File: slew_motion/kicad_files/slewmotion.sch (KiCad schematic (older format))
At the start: 115 parts

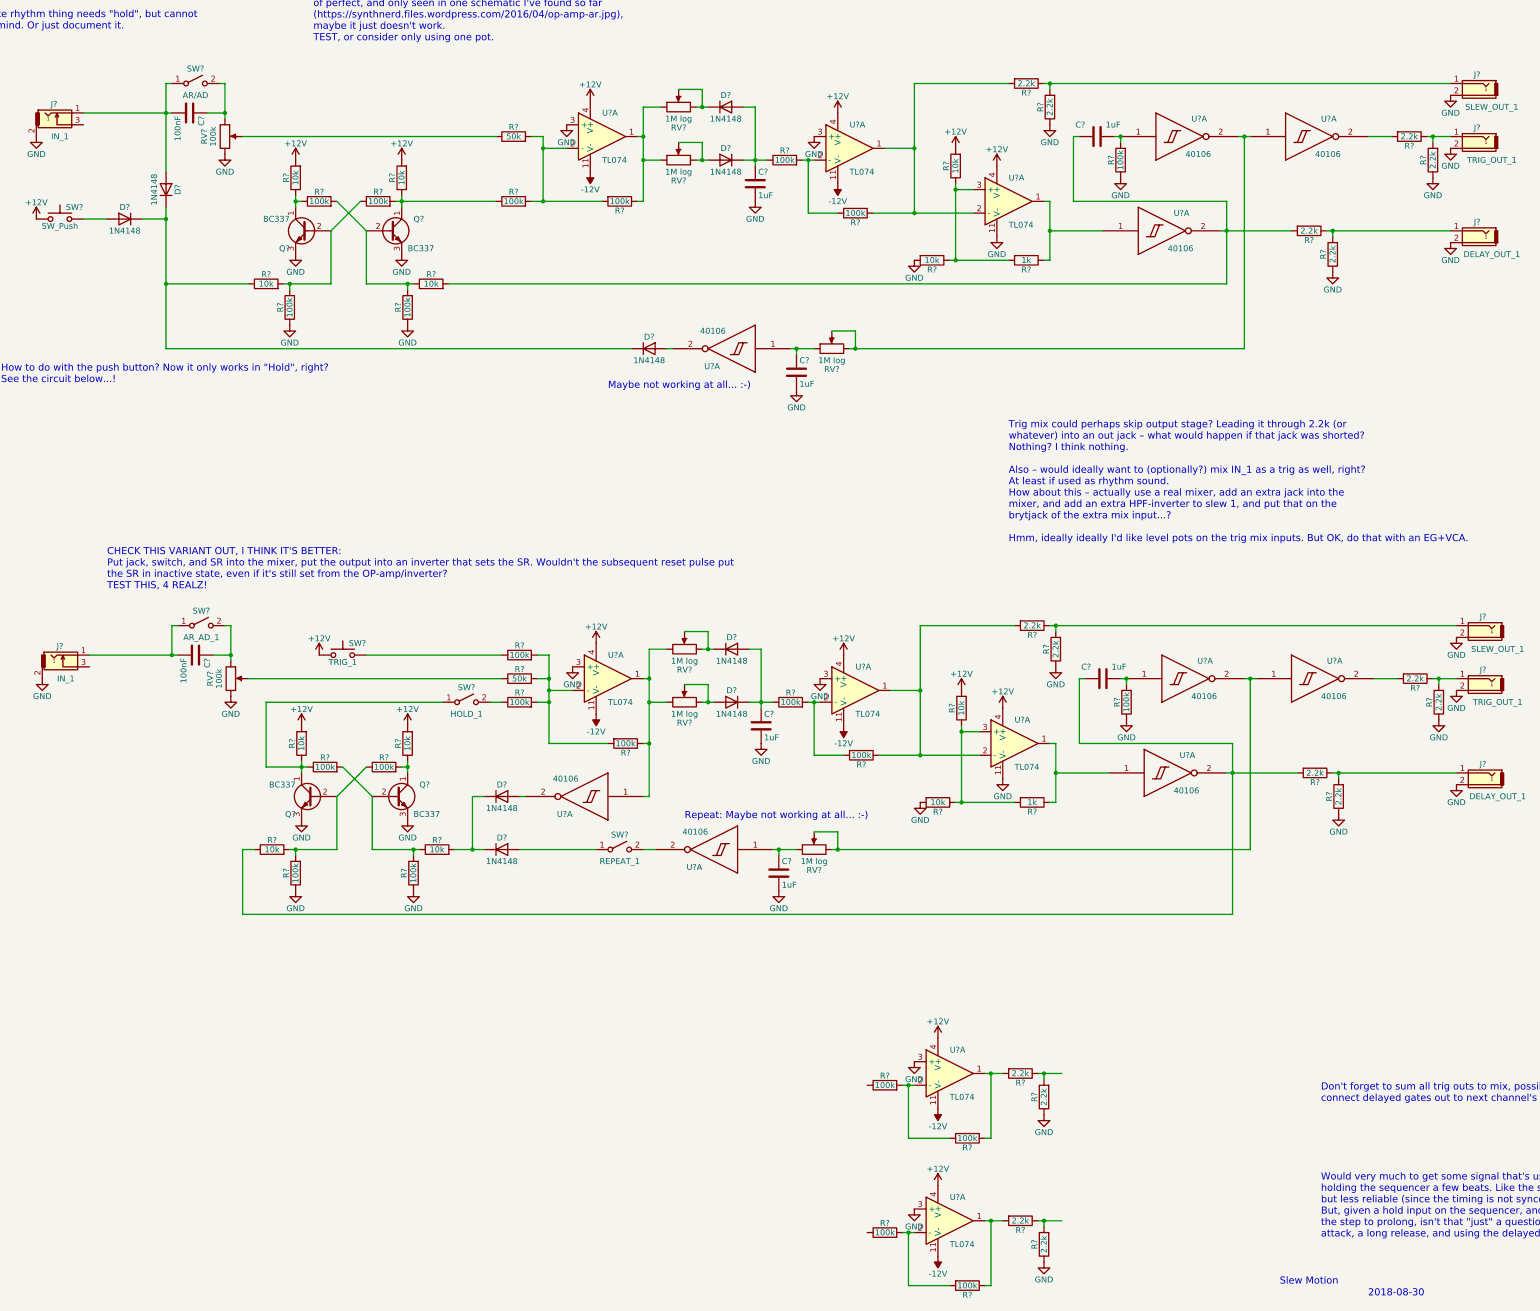
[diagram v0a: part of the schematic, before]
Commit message: Stuff that was left on my old computer (KiCad 4)
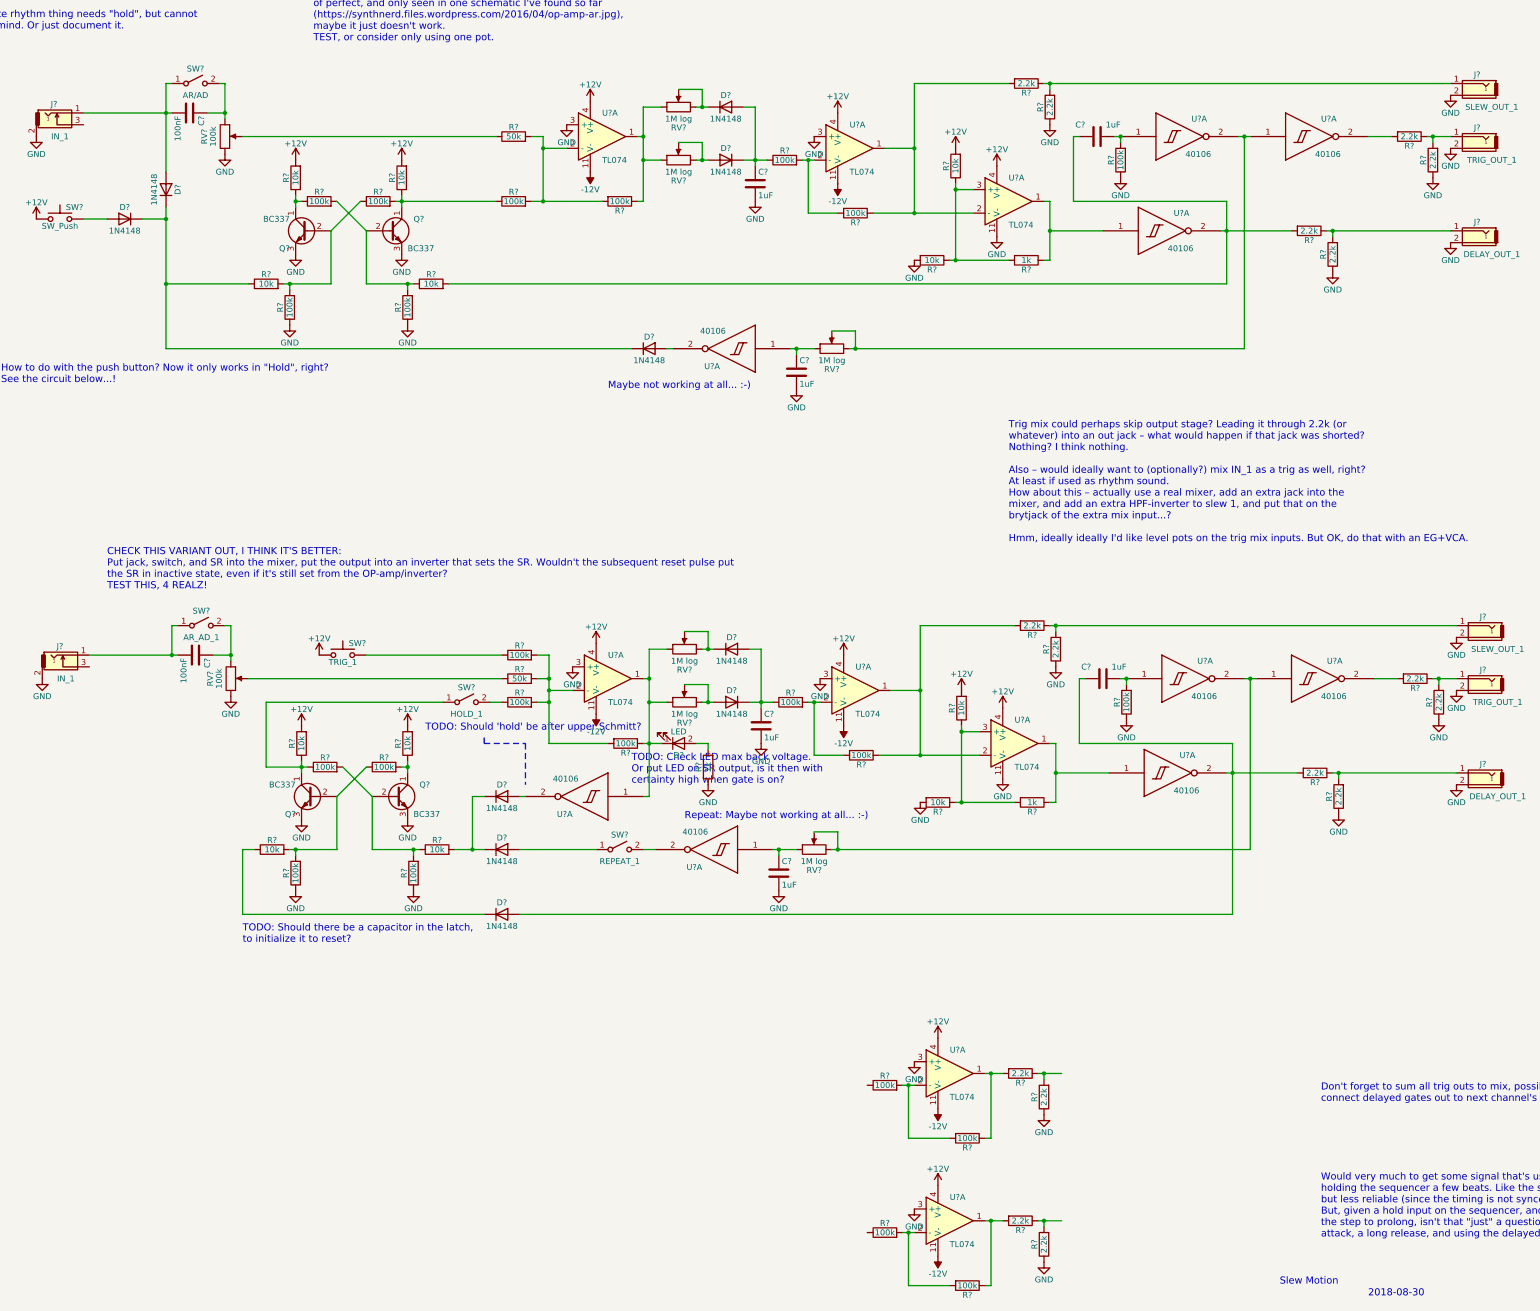
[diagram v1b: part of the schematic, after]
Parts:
- added D?: LED, symbol LED
- added D?: 1N4148, Diodes_THT:D_DO-35_SOD27_Horizontal_RM10, symbol 1N4148
- added R?: 1k, symbol R
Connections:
- net GND: now also R?.1
- net at R?.1, RV?.1, RV?.1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: now also D?.1 (K)
- net at C?.1, R?.2, U?.2 (Out): now also D?.2 (A); no longer R?.1
- new net: D?.1 (K), R?.1
- new net: D?.2 (A), R?.2
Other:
- note added: "TODO: Check LED max back voltage.\nOr put LED on SR output, is it then with \ncertainty high when gate is on?"
- note added: "TODO: Should 'hold' be after upper Schmitt?"
- note added: "TODO: Should there be a capacitor in the latch, \nto initialize it to reset?"
